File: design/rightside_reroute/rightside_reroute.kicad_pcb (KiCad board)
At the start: 4 copper layers, 144 x 96.2 mm, 198 parts, among them IC2 XC9148G50CER-G, IC3 nRF52833-QDAA-R7, IC4 74AHCT125PW,118, IC5 MCP23018T-E_SS, IC6 XC9291B33D1R-G, J1 USB_C_Receptacle_USB2.0_16P, J2 Battery Pos, J3 Battery Neg, J4 OLED_128x32, J6 Conn_01x04, J7 F32Q-1A7H1-11012, U1 BQ27441-G1, U2 BQ24072RGT, U3 USB6B1, U5 PEC11L-4015F-S0015, U6 PEC11L-4015F-S0015, Y1 ECS-320-8-37B2-JTY-TR

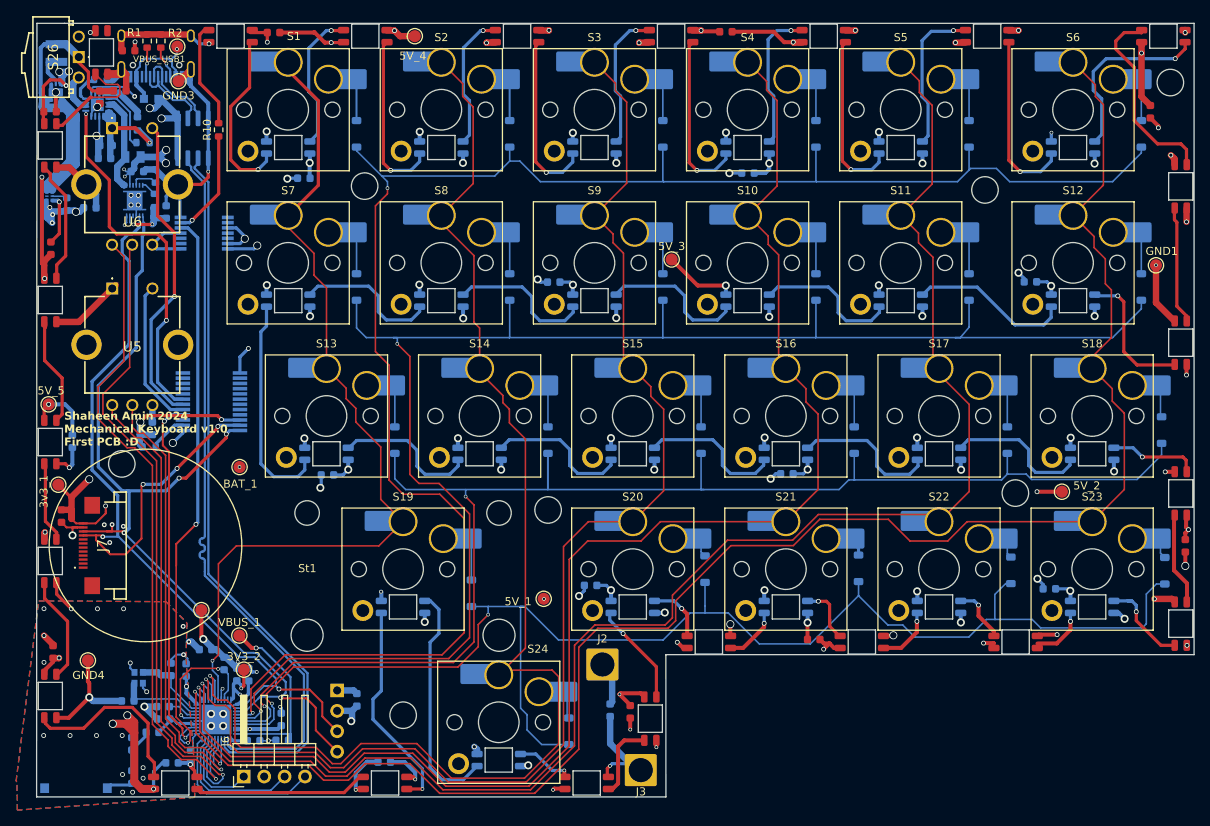
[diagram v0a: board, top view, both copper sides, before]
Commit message: scaling and positioning
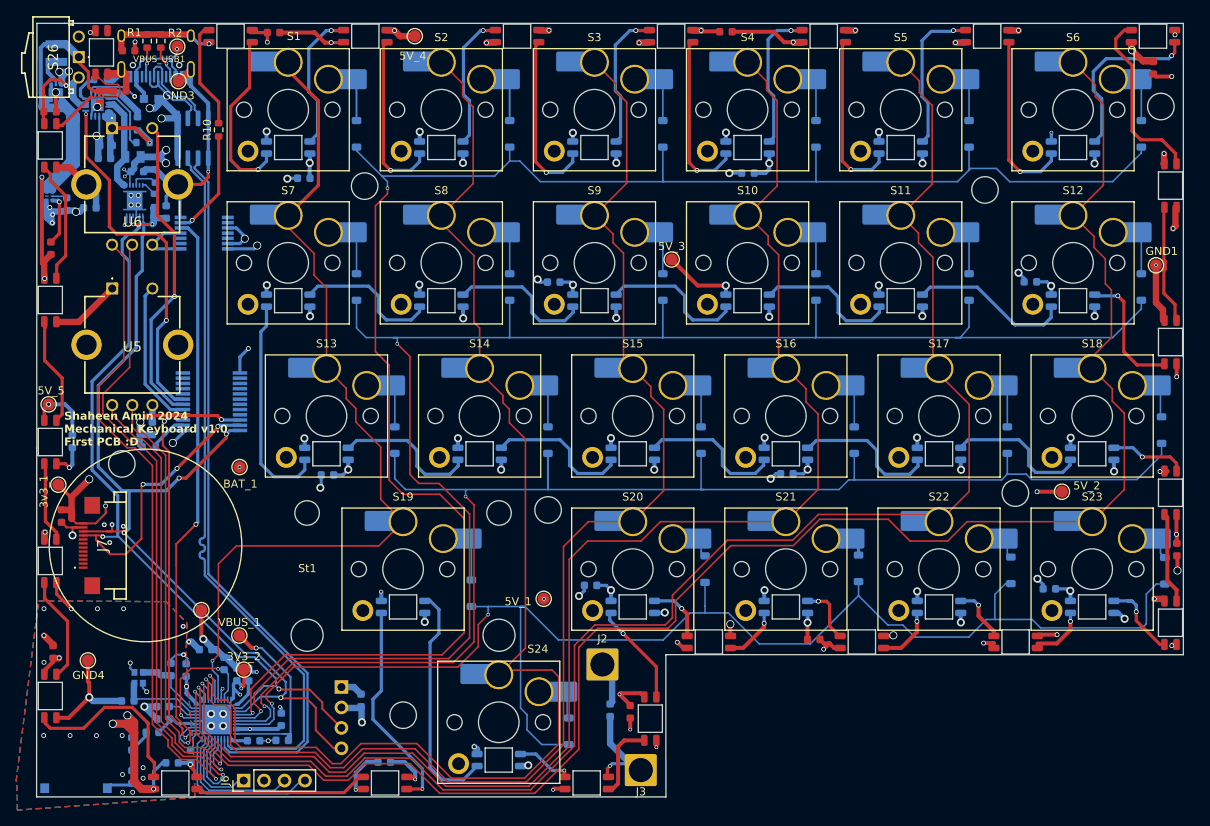
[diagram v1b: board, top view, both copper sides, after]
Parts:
- J6: footprint Connector_PinHeader_2.54mm:PinHeader_1x04_P2.54mm_Horizontal -> Connector_PinHeader_2.54mm:PinHeader_1x04_P2.54mm_Vertical
- moved C35 5.48 mm to (230.5, 42.2)
- moved REF** 3.21 mm to (231.4, 47.0)
- moved D13 1.29 mm to (230.4, 38.2)
- moved D29 1.27 mm to (232.6, 111.2)
- moved D14 1.27 mm to (232.6, 56.8)
- moved D15 1.27 mm to (232.6, 76.3)
- moved D28 1.27 mm to (232.6, 95.0)
- moved C36 1.15 mm to (233.4, 102.1)
- moved J4 0.68 mm to (131.1, 129.0)
- moved C9 0.52 mm to (131.9, 120.9)
- moved J6 0.50 mm to (117.3, 130.8)
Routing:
- net Net-(D13-DOUT): track 24.5 -> 22.5 mm
- net Net-(D27-DOUT): track 11.1 -> 9.56 mm
- net 5V: track 167.9 -> 166.4 mm
- net Net-(D15-DOUT): track 17.2 -> 15.8 mm
- net Net-(D29-DOUT): track 11.3 -> 9.99 mm
- net Net-(D12-DOUT): track 22.6 -> 21.9 mm
- net GND: track 318.5 -> 317.8 mm
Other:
- board size 144 x 96.2 mm -> 142.6 x 96.2 mm
